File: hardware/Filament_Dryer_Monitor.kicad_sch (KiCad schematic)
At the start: 0 parts

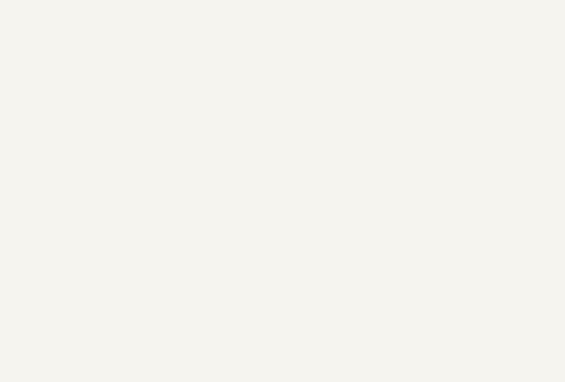
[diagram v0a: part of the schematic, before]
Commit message: Add L7987L buck redesign schematic with AutoEN protection
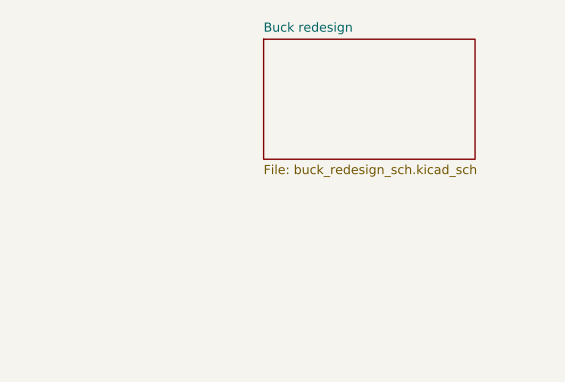
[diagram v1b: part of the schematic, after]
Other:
- added sheet Buck redesign (buck_redesign_sch.kicad_sch)
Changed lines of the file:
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@@
 	(paper "A4")
+	(sheet
+		(at 198.755 32.385)
+		(size 23.495 13.335)
+		(exclude_from_sim no)
+		(in_bom yes)
+		(on_board yes)
+		(dnp no)
+		(fields_autoplaced yes)
+		(stroke
+			(width 0.1524)
+			(type solid)
+		)
+		(fill
+			(color 0 0 0 0)
+		)
+		(property "Sheetname" "Buck redesign"
+			(at 198.755 31.6734 0)
+			(show_name no)
+			(do_not_autoplace no)
+			(effects
+				(font
+					(size 1.016 1.016)
+				)
+				(justify left bottom)
+			)
+		)
+		(property "Sheetfile" "buck_redesign_sch.kicad_sch"
+			(at 198.755 46.3046 0)
+			(show_name no)
+			(do_not_autoplace no)
+			(effects
+				(font
+					(size 1.016 1.016)
+				)
+				(justify left top)
+			)
+		)
+		(instances
+			(project "Filament_Dryer_Monitor"
+				(path "/ec014e20-abe2-47eb-baf0-3a9eae5bda3f"
+					(page "5")
+				)
+			)
+		)
+	)
 	(sheet
 		(at 80.01 77.47)

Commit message: Updated power schematic, delated buck schematic
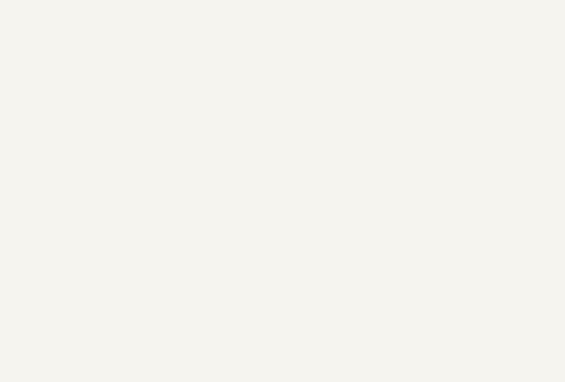
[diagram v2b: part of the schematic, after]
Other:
- removed sheet Buck redesign
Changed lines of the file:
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@@
 	(paper "A4")
-	(sheet
-		(at 198.755 32.385)
-		(size 23.495 13.335)
-		(exclude_from_sim no)
-		(in_bom yes)
-		(on_board yes)
-		(dnp no)
-		(fields_autoplaced yes)
-		(stroke
-			(width 0.1524)
-			(type solid)
-		)
-		(fill
-			(color 0 0 0 0)
-		)
-		(property "Sheetname" "Buck redesign"
-			(at 198.755 31.6734 0)
-			(show_name no)
-			(do_not_autoplace no)
-			(effects
-				(font
-					(size 1.016 1.016)
-				)
-				(justify left bottom)
-			)
-		)
-		(property "Sheetfile" "buck_redesign_sch.kicad_sch"
-			(at 198.755 46.3046 0)
-			(show_name no)
-			(do_not_autoplace no)
-			(effects
-				(font
-					(size 1.016 1.016)
-				)
-				(justify left top)
-			)
-		)
-		(instances
-			(project "Filament_Dryer_Monitor"
-				(path "/ec014e20-abe2-47eb-baf0-3a9eae5bda3f"
-					(page "5")
-				)
-			)
-		)
-	)
 	(sheet
 		(at 80.01 77.47)
